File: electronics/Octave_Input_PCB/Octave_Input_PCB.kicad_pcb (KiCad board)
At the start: 2 copper layers, 86.4 x 95.9 mm, 38 parts, among them SW1 SW_Hot_Swap_Socket, SW10 SW_Hot_Swap_Socket, SW11 SW_Hot_Swap_Socket, SW12 SW_Hot_Swap_Socket, SW13 SW_Hot_Swap_Socket, SW14 Alps_Alpine_RKJXV1224, SW15 Bourns_PEC12R-4xxxF-Sxxx, SW2 SW_Hot_Swap_Socket, SW3 SW_Hot_Swap_Socket, SW4 SW_Hot_Swap_Socket, SW5 SW_Hot_Swap_Socket, SW6 SW_Hot_Swap_Socket, SW7 SW_Hot_Swap_Socket, SW8 SW_Hot_Swap_Socket, SW9 SW_Hot_Swap_Socket, U1 Adafruit_QT_Py_RP2040, U2 Raspberry_Pi_RP2040

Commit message: [WIP] Update schematic and PCB
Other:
- board size 86.4 x 95.9 mm -> 87.8 x 95.8 mm
- board text added: "Octave Input PCB rev.5.a"
- board text removed: "Octave Input PCB rev.4"
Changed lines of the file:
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@@
   (title_block
     (title "Octave - Input PCB")
-    (date "2022-05-05")
+    (date "2022-05-06")
     (rev "5.a")
     (comment 4 "https://github.com/takayoshiotake/octave-12-key-macropad")
@@
     )
   )
-  (gr_line (start 123.825 42.545) (end 50.165 42.545) (layer "Edge.Cuts") (width 0.1))
-  (gr_line (start 47.625 138.43) (end 123.825 138.43) (layer "Edge.Cuts") (width 0.1))
-  (gr_arc (start 47.625 138.43) (mid 44.032898 136.942102) (end 42.545 133.35) (layer "Edge.Cuts") (width 0.1))
-  (gr_line (start 50.165 42.545) (end 47.625 42.545) (layer "Edge.Cuts") (width 0.1))
-  (gr_arc (start 128.905 133.35) (mid 127.417102 136.942102) (end 123.825 138.43) (layer "Edge.Cuts") (width 0.1))
-  (gr_arc (start 42.545 47.625) (mid 44.032898 44.032898) (end 47.625 42.545) (layer "Edge.Cuts") (width 0.1))
-  (gr_arc (start 123.825 42.545) (mid 127.417102 44.032898) (end 128.905 47.625) (layer "Edge.Cuts") (width 0.1))
-  (gr_line (start 128.905 133.35) (end 128.905 47.625) (layer "Edge.Cuts") (width 0.1))
-  (gr_line (start 42.545 47.625) (end 42.545 133.35) (layer "Edge.Cuts") (width 0.1))
-  (gr_rect (start 37.725 37.725) (end 133.725 143.25) (layer "F.Fab") (width 0.12) (fill none))
+  (gr_rect (start 41.825 41.825) (end 129.625 137.625) (layer "Cmts.User") (width 0.15) (fill none))
+  (gr_rect (start 41.825 41.825) (end 49.625 49.625) (layer "Cmts.User") (width 0.15) (fill none))
+  (gr_rect (start 121.825 129.825) (end 129.625 137.625) (layer "Cmts.User") (width 0.15) (fill none))
+  (gr_rect (start 121.825 41.825) (end 129.625 49.625) (layer "Cmts.User") (width 0.15) (fill none))
+  (gr_rect (start 41.825 129.825) (end 49.625 137.625) (layer "Cmts.User") (width 0.15) (fill none))
+  (gr_arc (start 121.825 41.825) (mid 127.340433 44.109567) (end 129.625 49.625) (layer "Edge.Cuts") (width 0.1))
+  (gr_arc (start 129.625 129.825) (mid 127.340433 135.340433) (end 121.825 137.625) (layer "Edge.Cuts") (width 0.1))
+  (gr_arc (start 41.825 49.625) (mid 44.109567 44.109567) (end 49.625 41.825) (layer "Edge.Cuts") (width 0.1))
+  (gr_line (start 121.825 41.825) (end 49.625 41.825) (layer "Edge.Cuts") (width 0.1))
+  (gr_line (start 41.825 49.625) (end 41.825 129.825) (layer "Edge.Cuts") (width 0.1))
+  (gr_line (start 49.625 137.625) (end 121.825 137.625) (layer "Edge.Cuts") (width 0.1))
+  (gr_line (start 129.625 129.825) (end 129.625 49.625) (layer "Edge.Cuts") (width 0.1))
+  (gr_arc (start 49.625 137.625) (mid 44.109567 135.340433) (end 41.825 129.825) (layer "Edge.Cuts") (width 0.1))
   (gr_rect (start 76.2 114.3) (end 95.25 133.35) (layer "F.Fab") (width 0.15) (fill none))
   (gr_rect (start 47.625 104.775) (end 66.675 123.825) (layer "F.Fab") (width 0.15) (fill none))
-  (gr_text "JLCJLCJLCJLC" (at 114.3 135.89) (layer "F.SilkS")
-    (effects (font (size 1 1) (thickness 0.15)))
-  )
-  (gr_text "Octave Input PCB rev.4" (at 57.15 135.89) (layer "F.SilkS")
-    (effects (font (size 1 1) (thickness 0.15)))
+  (gr_text "JLCJLCJLCJLC" (at 120.725 135.725) (layer "F.SilkS")
+    (effects (font (size 1 1) (thickness 0.15)) (justify right))
+  )
+  (gr_text "Octave Input PCB rev.5.a" (at 50.725 135.725) (layer "F.SilkS")
+    (effects (font (size 1 1) (thickness 0.15)) (justify left))
   )
   (dimension (type aligned) (layer "Cmts.User")
-    (pts (xy 42.545 47.625) (xy 128.905 47.625))
-    (height -14.605)
-    (gr_text "3.4000 in" (at 85.725 31.87) (layer "Cmts.User")
-      (effects (font (size 1 1) (thickness 0.15)))
-    )
-    (format (units 0) (units_format 1) (precision 4))
+    (pts (xy 49.625 49.625) (xy 44.109567 44.109567))
+    (height -15.715448)
+    (gr_text "7.8 mm" (at 36.567957 57.166611 -45) (layer "Cmts.User")
+      (effects (font (size 1 1) (thickness 0.15)))
+    )
+    (format (units 3) (units_format 1) (precision 1))
     (style (thickness 0.15) (arrow_length 1.27) (text_position_mode 0) (extension_height 0.58642) (extension_offset 0.5) keep_text_aligned)
   )
   (dimension (type aligned) (layer "Cmts.User")
-    (pts (xy 123.19 42.545) (xy 123.19 138.43))
-    (height -15.24)
-    (gr_text "3.7750 in" (at 137.28 90.4875 90) (layer "Cmts.User")
-      (effects (font (size 1 1) (thickness 0.15)))
-    )
-    (format (units 0) (units_format 1) (precision 4))
+    (pts (xy 129.625 41.825) (xy 129.625 137.625))
+    (height -30.395)
+    (gr_text "95.8 mm" (at 158.87 89.725 90) (layer "Cmts.User")
+      (effects (font (size 1 1) (thickness 0.15)))
+    )
+    (format (units 3) (units_format 1) (precision 1))
     (style (thickness 0.15) (arrow_length 1.27) (text_position_mode 0) (extension_height 0.58642) (extension_offset 0.5) keep_text_aligned)
   )
+  (dimension (type aligned) (layer "Cmts.User")
+    (pts (xy 41.825 41.825) (xy 129.625 41.825))
+    (height -5.63)
+    (gr_text "87.8 mm" (at 85.725 35.045) (layer "Cmts.User")
+      (effects (font (size 1 1) (thickness 0.15)))
+    )
+    (format (units 3) (units_format 1) (precision 1))
+    (style (thickness 0.15) (arrow_length 1.27) (text_position_mode 0) (extension_height 0.58642) (extension_offset 0.5) keep_text_aligned)
+  )

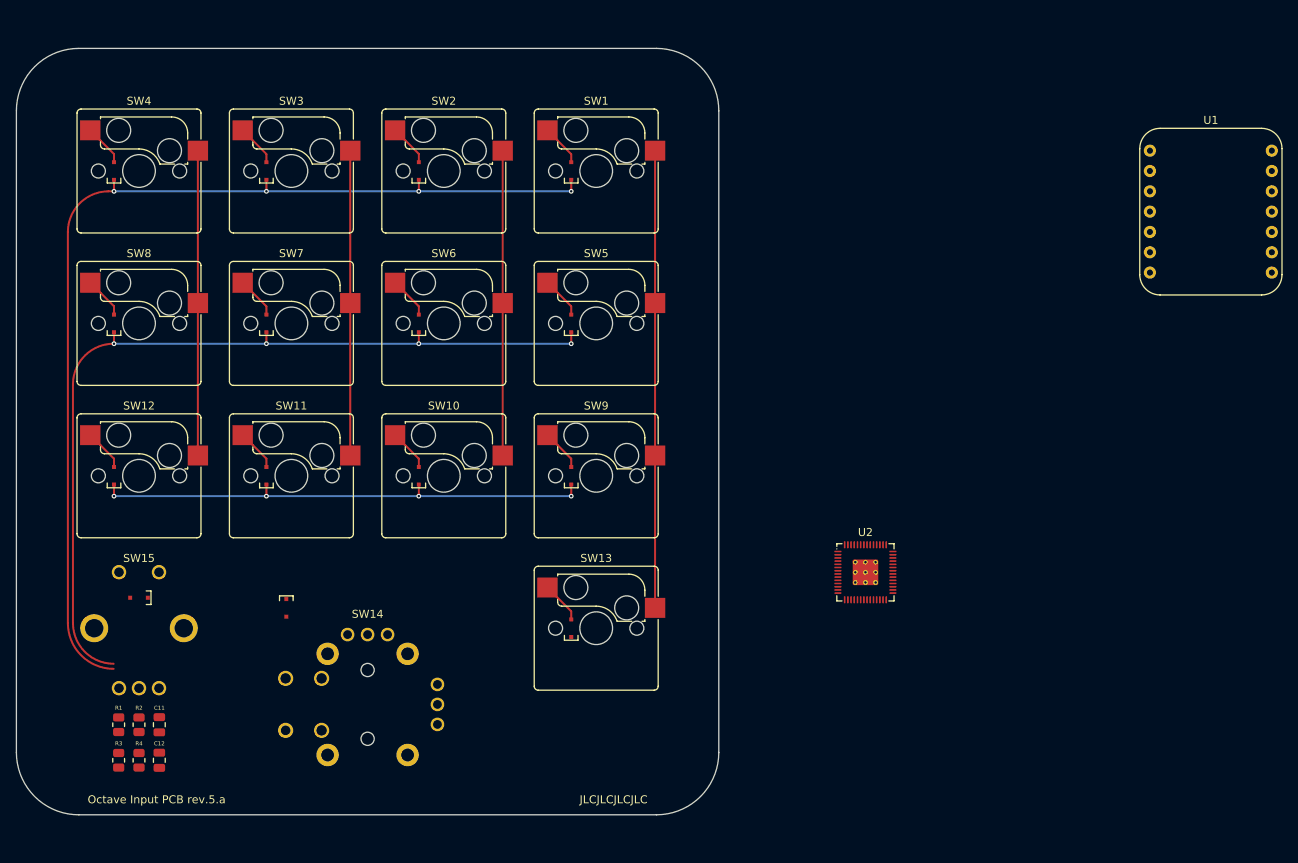
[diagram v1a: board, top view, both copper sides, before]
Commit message: [WIP] Update schematic and PCB
Add a USB-C connector, but using the Molex 1054500101 makes routing very difficult.
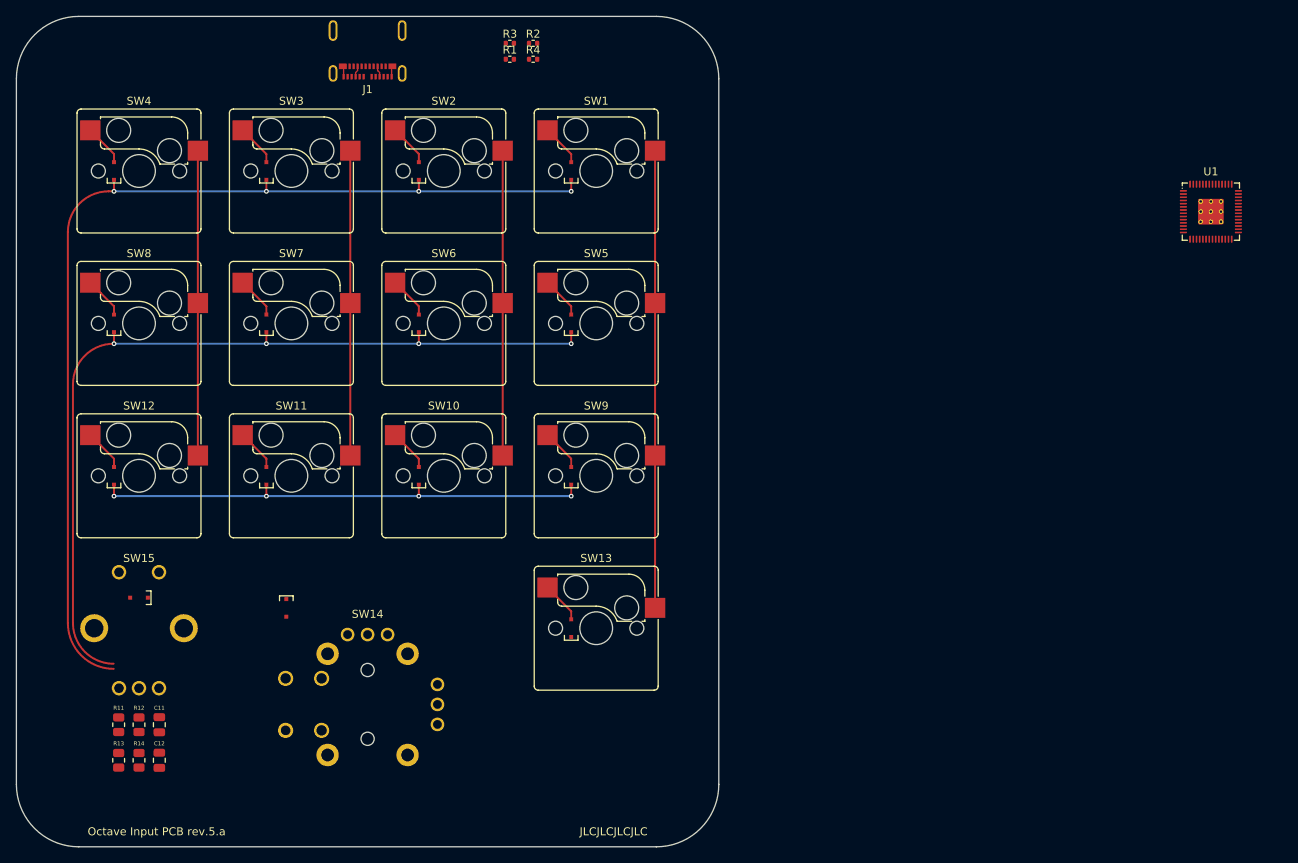
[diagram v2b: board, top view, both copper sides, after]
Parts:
- removed U2: Raspberry_Pi_RP2040, Octave_Library:RP2040_QFN-56
- added J1: Molex_USB-C-SMD_1054500101, Octave_Library:Molex_USB-C-SMD_1054500101, F.Cu at (85.7, 42.5)
- added R1: 5.1K, Resistor_SMD:R_0402_1005Metric, F.Cu at (103.5, 43.2)
- added R2: 5.1K, Resistor_SMD:R_0402_1005Metric, F.Cu at (106.4, 41.2)
- added R3: 27, Resistor_SMD:R_0402_1005Metric, F.Cu at (103.5, 41.2)
- added R4: 27, Resistor_SMD:R_0402_1005Metric, F.Cu at (106.4, 43.2)
- U1: value Adafruit_QT_Py_RP2040 -> Raspberry_Pi_RP2040; footprint Octave_Library:Adafruit_QT_Py_RP2040 -> Octave_Library:RP2040_QFN-56
- renumbered R1 to R11, R2 to R12, R3 to R13, R4 to R14
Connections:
- U1 pad 1: col2 -> unconnected-(U1-Pad1)
- U1 pad 11: SignalB -> unconnected-(U1-Pad11)
- U1 pad 12: +3V3 -> unconnected-(U1-Pad12)
- U1 pad 13: GND -> unconnected-(U1-Pad13)
- U1 pad 2: col1 -> unconnected-(U1-Pad2)
- U1 pad 3: col0 -> unconnected-(U1-Pad3)
- U1 pad 4: row2 -> unconnected-(U1-Pad4)
- U1 pad 5: col3 -> unconnected-(U1-Pad5)
- U1 pad 6: row1 -> unconnected-(U1-Pad6)
- U1 pad 7: row0 -> unconnected-(U1-Pad7)
- U1 pad 8: row3 -> unconnected-(U1-Pad8)
- U1 pad 9: SignalA -> unconnected-(U1-Pad9)
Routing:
- net +5V: track 0.00 -> 2.81 mm
- net GND: track 0.00 -> 2.68 mm
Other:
- board size 87.8 x 95.8 mm -> 87.8 x 103.8 mm

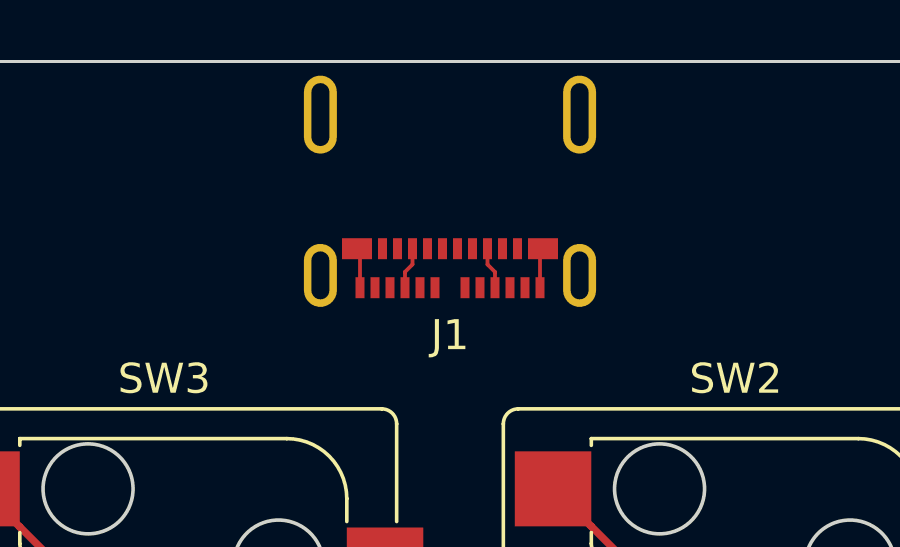
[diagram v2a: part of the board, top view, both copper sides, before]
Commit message: Change the USB-C connector to HRO TYPE-C-31-M-12
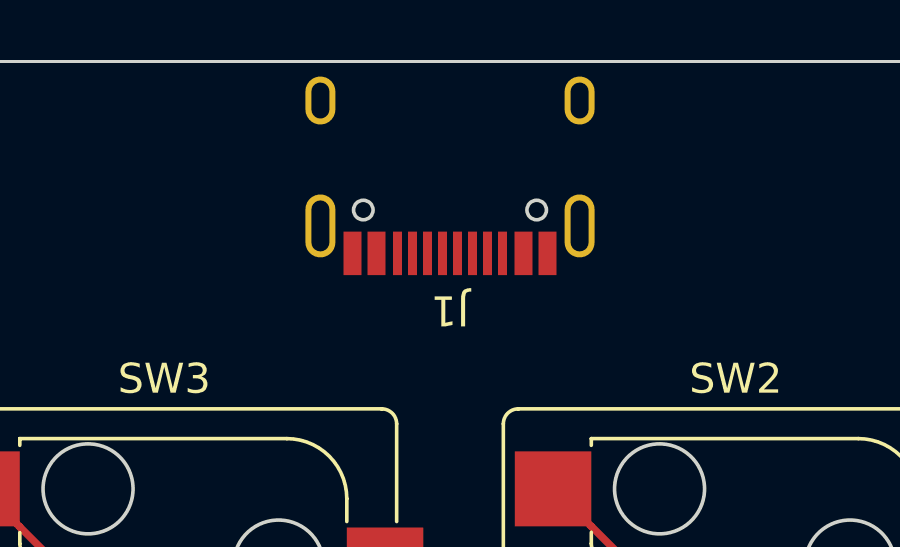
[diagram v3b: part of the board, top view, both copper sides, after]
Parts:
- J1: value Molex_USB-C-SMD_1054500101 -> HRO_TYPE-C-31-M-12; footprint Octave_Library:Molex_USB-C-SMD_1054500101 -> Octave_Library:HRO_TYPE-C-31-M-12
- moved J1 0.83 mm to (85.7, 41.7)
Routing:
- net +5V: track 2.81 -> 0.00 mm
- net GND: track 2.68 -> 0.00 mm

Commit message: [WIP] Update schematic and PCB
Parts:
- moved U1 113.7 mm to (85.7, 104.8)
- moved R4 21.6 mm to (86.0, 50.3), turned to 90 degrees
- moved R2 21.5 mm to (87.0, 50.3), turned to -90 degrees
- moved R1 20.8 mm to (84.0, 50.3), turned to -90 degrees
- moved R3 20.6 mm to (85.0, 50.3), turned to 90 degrees
- moved J1 4.00 mm to (85.7, 45.7)
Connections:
- J1 pad A5: Net-(R1-Pad1) -> Net-(J1-PadA5)
- J1 pad B5: Net-(R2-Pad1) -> Net-(J1-PadB5)
- R1 pad 1: Net-(R1-Pad1) -> Net-(J1-PadB5)
- R2 pad 1: Net-(R2-Pad1) -> Net-(J1-PadA5)
- R3 pad 1: unconnected-(R3-Pad1) -> D+
- R4 pad 1: unconnected-(R4-Pad1) -> D-
- U1 pad 46: unconnected-(U1-Pad46) -> D-
- U1 pad 47: unconnected-(U1-Pad47) -> D+
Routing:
- net D+: track 0.00 -> 51.3 mm
- net D-: track 0.00 -> 51.0 mm
- net +5V: track 0.00 -> 7.03 mm
- net Net-(J1-PadA6): track 0.00 -> 5.05 mm
- net Net-(J1-PadA7): track 0.00 -> 4.70 mm
- net Net-(J1-PadB5): track 0.00 -> 1.43 mm
- net Net-(J1-PadA5): track 0.00 -> 1.43 mm
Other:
- board size 87.8 x 103.8 mm -> 87.8 x 95.8 mm

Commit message: [WIP] Update schematic and PCB
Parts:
- added C1: 1uF, Capacitor_SMD:C_0402_1005Metric, F.Cu at (83.6, 61.5)
- added C10: 0.1uF, Capacitor_SMD:C_0402_1005Metric, F.Cu at (84.7, 97.8)
- added C11: 0.1uF, Capacitor_SMD:C_0402_1005Metric, F.Cu at (86.9, 110.8)
- added C12: 0.1uF, Capacitor_SMD:C_0402_1005Metric, F.Cu at (83.7, 97.8)
- added C13: 1uF, Capacitor_SMD:C_0402_1005Metric, F.Cu at (85.7, 97.8)
- added C14: 1uF, Capacitor_SMD:C_0402_1005Metric, F.Cu at (91.8, 101.0)
- added C2: 1uF, Capacitor_SMD:C_0402_1005Metric, F.Cu at (83.6, 66.8)
- added C3: 1uF, Capacitor_SMD:C_0402_1005Metric, F.Cu at (89.7, 98.4)
- added C4: 1uF, Capacitor_SMD:C_0402_1005Metric, F.Cu at (88.7, 98.4)
- added C5: 0.1uF, Capacitor_SMD:C_0402_1005Metric, F.Cu at (79.7, 102.2)
- added C6: 0.1uF, Capacitor_SMD:C_0402_1005Metric, F.Cu at (79.7, 105.8)
- added C7: 0.1uF, Capacitor_SMD:C_0402_1005Metric, F.Cu at (85.9, 110.8)
- added C8: 0.1uF, Capacitor_SMD:C_0402_1005Metric, F.Cu at (91.7, 105.8)
- added C9: 0.1uF, Capacitor_SMD:C_0402_1005Metric, F.Cu at (91.7, 102.2)
- added U1: AP2112K-3.3, Package_TO_SOT_SMD:SOT-23-5, F.Cu at (83.2, 64.1)
- moved R3 48.2 mm to (86.7, 98.4)
- moved R4 48.2 mm to (87.7, 98.4)
- moved R1 0.07 mm to (84.0, 50.2)
- moved R2 0.07 mm to (87.0, 50.2)
- renumbered C11 to C21, C12 to C22, U1 to U2
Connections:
- U2 pad 1: unconnected-(U1-Pad1) -> +3V3
- U2 pad 10: unconnected-(U1-Pad10) -> +3V3
- U2 pad 19: unconnected-(U1-Pad19) -> GND
- U2 pad 22: unconnected-(U1-Pad22) -> +3V3
- U2 pad 23: unconnected-(U1-Pad23) -> +1V1
- U2 pad 33: unconnected-(U1-Pad33) -> +3V3
- U2 pad 42: unconnected-(U1-Pad42) -> +3V3
- U2 pad 43: unconnected-(U1-Pad43) -> +3V3
- U2 pad 44: unconnected-(U1-Pad44) -> +3V3
- U2 pad 45: unconnected-(U1-Pad45) -> +1V1
- U2 pad 48: unconnected-(U1-Pad48) -> +3V3
- U2 pad 49: unconnected-(U1-Pad49) -> +3V3
- U2 pad 50: unconnected-(U1-Pad50) -> +1V1
- U2 pad 57: unconnected-(U1-Pad57) -> GND
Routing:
- net D-: track 51.0 -> 0.00 mm
- net D+: track 51.3 -> 2.41 mm
- net col2: track 38.1 -> 0.00 mm
- net +3V3: track 0.00 -> 8.24 mm
- net Net-(J1-PadA6): track 5.05 -> 3.17 mm
- net Net-(J1-PadA7): track 4.70 -> 3.17 mm
- net +1V1: track 0.00 -> 1.50 mm, vias 0 -> 2
